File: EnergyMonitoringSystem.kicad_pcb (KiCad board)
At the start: 6 copper layers, 170 x 117 mm, 202 parts, among them J201 USB_C_Receptacle_USB2.0_16P, J202 Screw_Terminal_01x02, J401 Conn_02x05_Counter_Clockwise, J402 Conn_02x05_Counter_Clockwise, J403 Conn_02x08_Counter_Clockwise, J501 Screw_Terminal_01x02, J502 Screw_Terminal_01x02, J503 Screw_Terminal_01x02, J504 Screw_Terminal_01x02, J505 Screw_Terminal_01x02, J506 Screw_Terminal_01x02, J601 DM3AT-SF-PEJM5_40_, J602 Screw_Terminal_01x03, Q201 STL6N3LLH6, SW401 SW_Push, SW402 SW_Push, U201 USBLC6-2P6, U202 STEF05SGR, U203 TCPP01-M12, U301 LDLN025M12R, U302 ST1PS02CQTR, U303 ST1PS02CQTR, U304 LM2664M6_NOPB, U401 STM32F103RGT6, U402 BLUENRG-M2SA, U501 ADS131M08IRSNR, U502 TSV914AIDR, U503 TSV914AIDR, U504 TSV914AIDR, U601 EMIF06-MSD02N16, U602 ADM2565EBRNZ, Y401 16MHz, Y402 32.768KHz

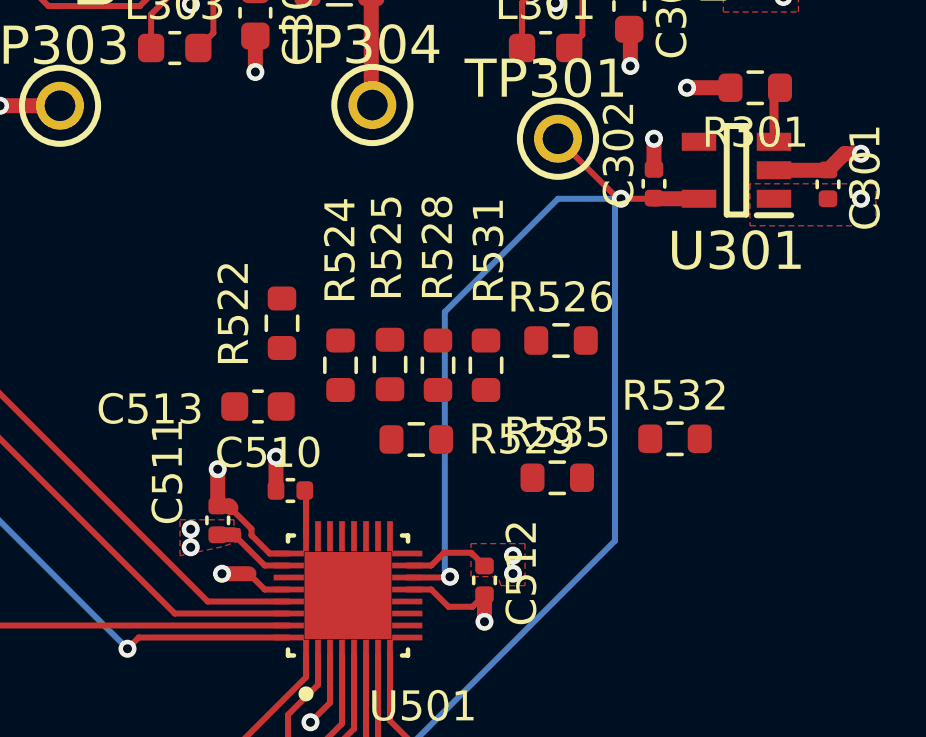
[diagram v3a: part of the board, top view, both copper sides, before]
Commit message: adc wiring complete
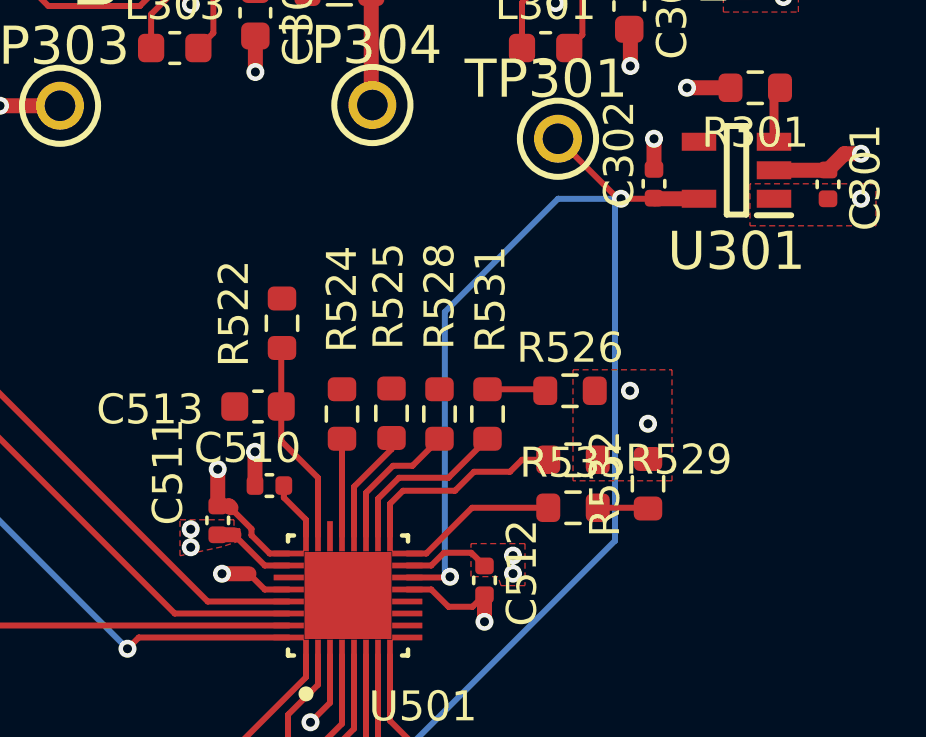
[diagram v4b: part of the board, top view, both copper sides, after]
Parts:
- moved R529 5.27 mm to (104.1, 86.7)
- moved R532 1.75 mm to (106.6, 87.5), turned to 90 degrees
- moved R526 1.70 mm to (104.0, 84.4)
- moved R524 1.63 mm to (96.4, 85.2)
- moved R528 1.63 mm to (99.7, 85.2)
- moved R525 1.63 mm to (98.0, 85.2)
- moved R531 1.63 mm to (101.2, 85.2)
- moved R535 1.13 mm to (104.1, 88.3)
- moved C510 0.72 mm to (94.0, 87.6)
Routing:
- net ADS_CS: track 0.00 -> 6.97 mm
- net /ADC/CLKIN_ADS_T: track 0.00 -> 6.79 mm
- net /ADC/DRDY_ADS_T: track 0.00 -> 5.73 mm
- net /ADC/SYNC_RESET_ADS_T: track 0.00 -> 5.33 mm
- net /ADC/SCK_ADS_T: track 0.00 -> 4.64 mm
- net /ADC/DOUT_ADS_T: track 0.00 -> 3.79 mm
- net /ADC/DIN_ADS_T: track 0.00 -> 3.25 mm
- net ADS_DRDY: track 0.00 -> 1.95 mm
- net ADS_SYNC_RESET: track 0.00 -> 1.69 mm
- net Net-(U501-CAP): track 1.54 -> 2.05 mm
- net +DCDC_1: vias 13 -> 15

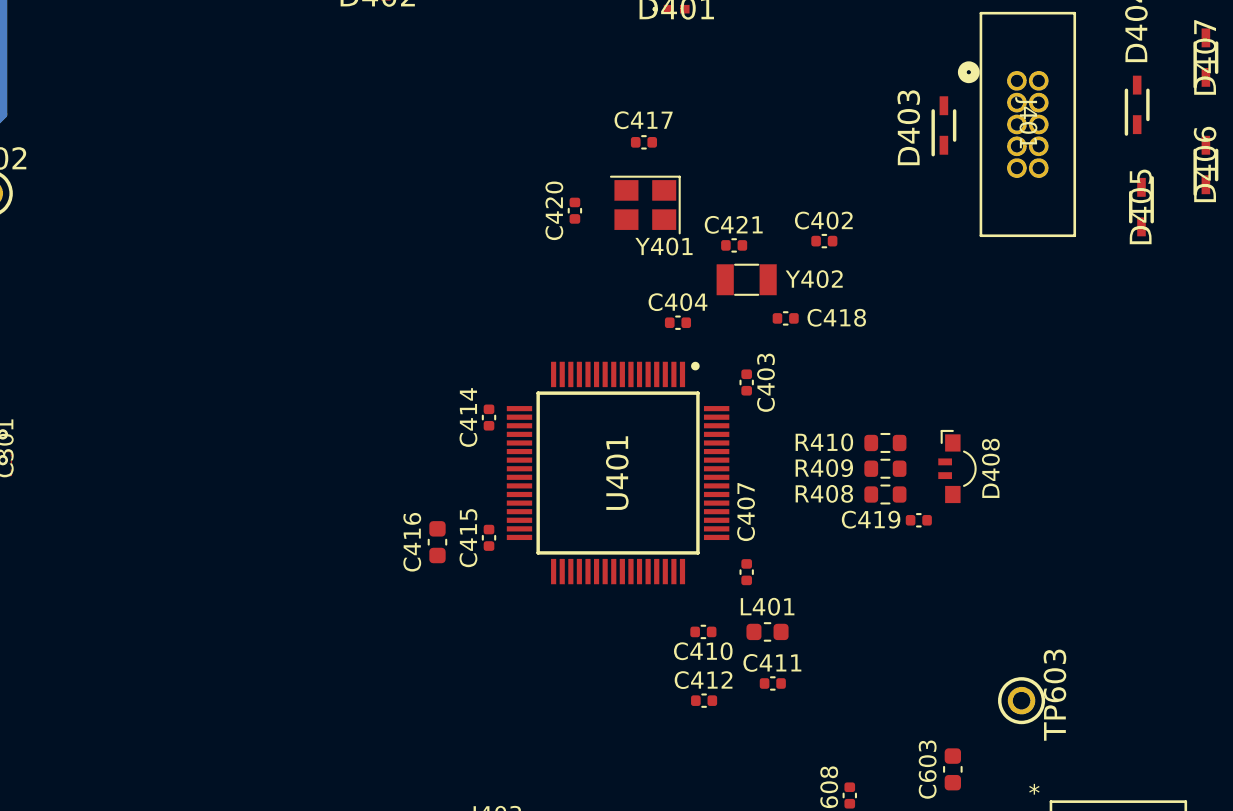
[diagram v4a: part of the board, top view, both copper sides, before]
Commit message: power supply to uC
1. Power supply complete
2. Crystal Oscillator complete
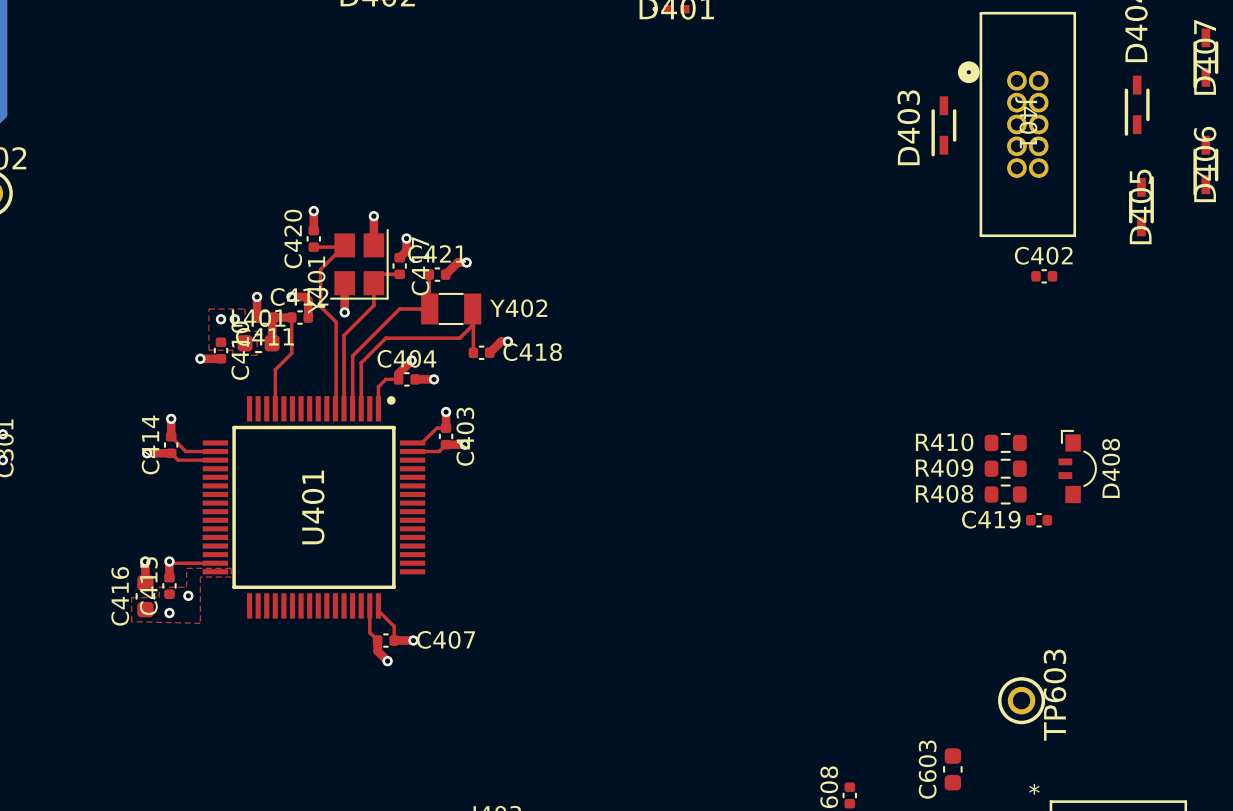
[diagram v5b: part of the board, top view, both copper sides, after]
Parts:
- moved C411 36.4 mm to (129.0, 69.7), turned to 180 degrees
- moved L401 34.1 mm to (128.6, 71.2)
- moved C410 32.5 mm to (126.4, 71.6), turned to -90 degrees
- moved C412 32.4 mm to (131.0, 69.7)
- moved C407 21.4 mm to (136.0, 88.5), turned to 180 degrees
- moved C415 18.8 mm to (123.4, 85.3)
- moved C414 18.6 mm to (123.5, 77.1)
- moved C418 17.8 mm to (141.6, 71.8)
- moved U401 17.8 mm to (131.8, 80.8)
- moved C403 17.8 mm to (139.5, 76.6)
- moved C421 17.4 mm to (139.0, 67.2)
- moved C416 17.3 mm to (122.0, 85.9)
- moved Y402 17.3 mm to (139.8, 69.2)
- moved Y401 17.0 mm to (134.4, 66.6), turned to 90 degrees
- moved C404 16.1 mm to (137.2, 73.3)
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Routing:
- net GND: track 238.3 -> 268.3 mm, vias 59 -> 74
- net +DCDC_1: track 18.3 -> 33.2 mm, vias 15 -> 23
- net /uC/OSC32_IN: track 0.00 -> 13.6 mm
- net /uC/OSC_OUT: track 0.00 -> 12.3 mm
- net /uC/OSC32_OUT: track 0.00 -> 10.7 mm
- net /uC/OSC_IN: track 0.00 -> 9.75 mm
- net VDDA: track 0.00 -> 8.30 mm

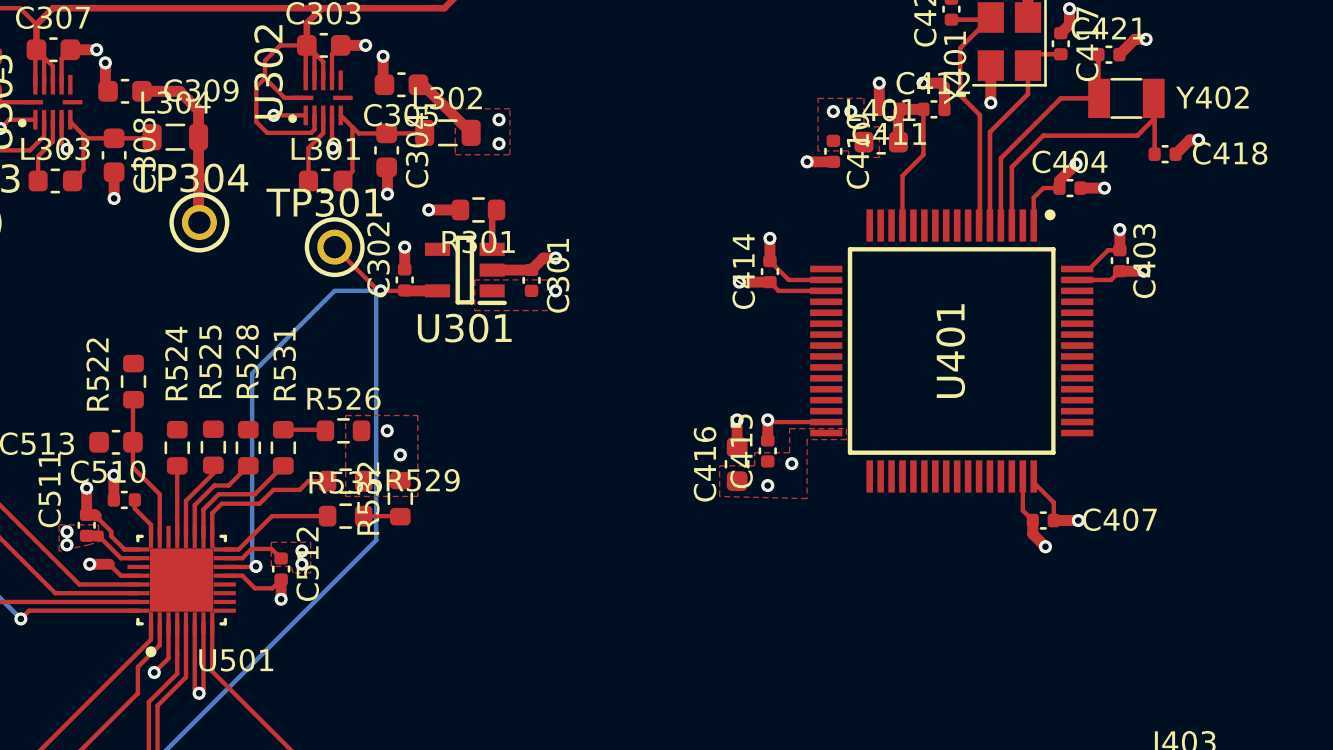
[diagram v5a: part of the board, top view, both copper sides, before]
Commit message: adc to uc complete
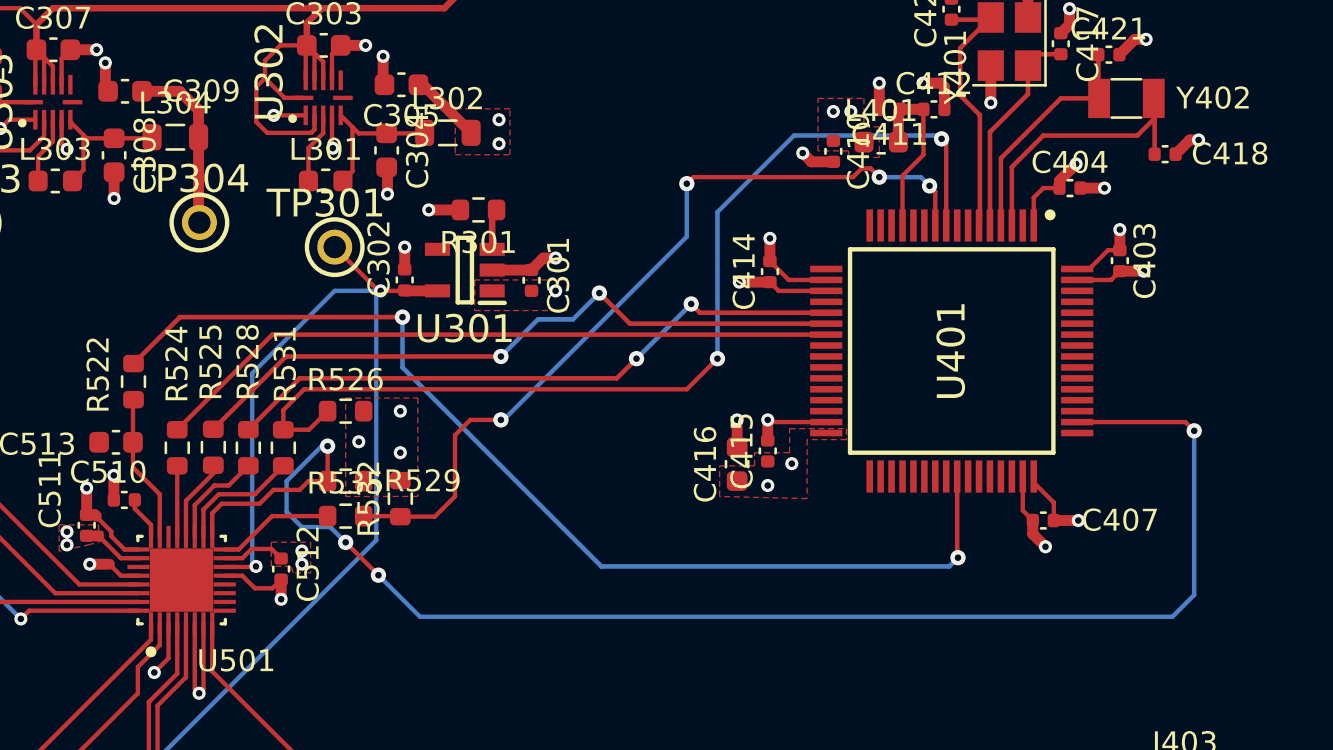
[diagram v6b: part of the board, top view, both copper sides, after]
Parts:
- moved R526 0.91 mm to (104.1, 83.5)
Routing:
- net ADS_CS: track 6.97 -> 69.4 mm, vias 0 -> 4
- net ADS_STM32_CLKOUT: track 0.00 -> 48.5 mm, vias 0 -> 2
- net ADS_DRDY: track 1.95 -> 46.6 mm, vias 0 -> 2
- net ADS_SYNC_RESET: track 1.69 -> 37.8 mm, vias 0 -> 4
- net ADS_DIN_uC_DOUT: track 0.00 -> 31.5 mm
- net ADS_DOUT_uC_DIN: track 0.00 -> 31.2 mm, vias 0 -> 2
- net ADS_SPI1_SCK: track 0.00 -> 29.0 mm, vias 0 -> 2
- net +DCDC_1: vias 23 -> 24

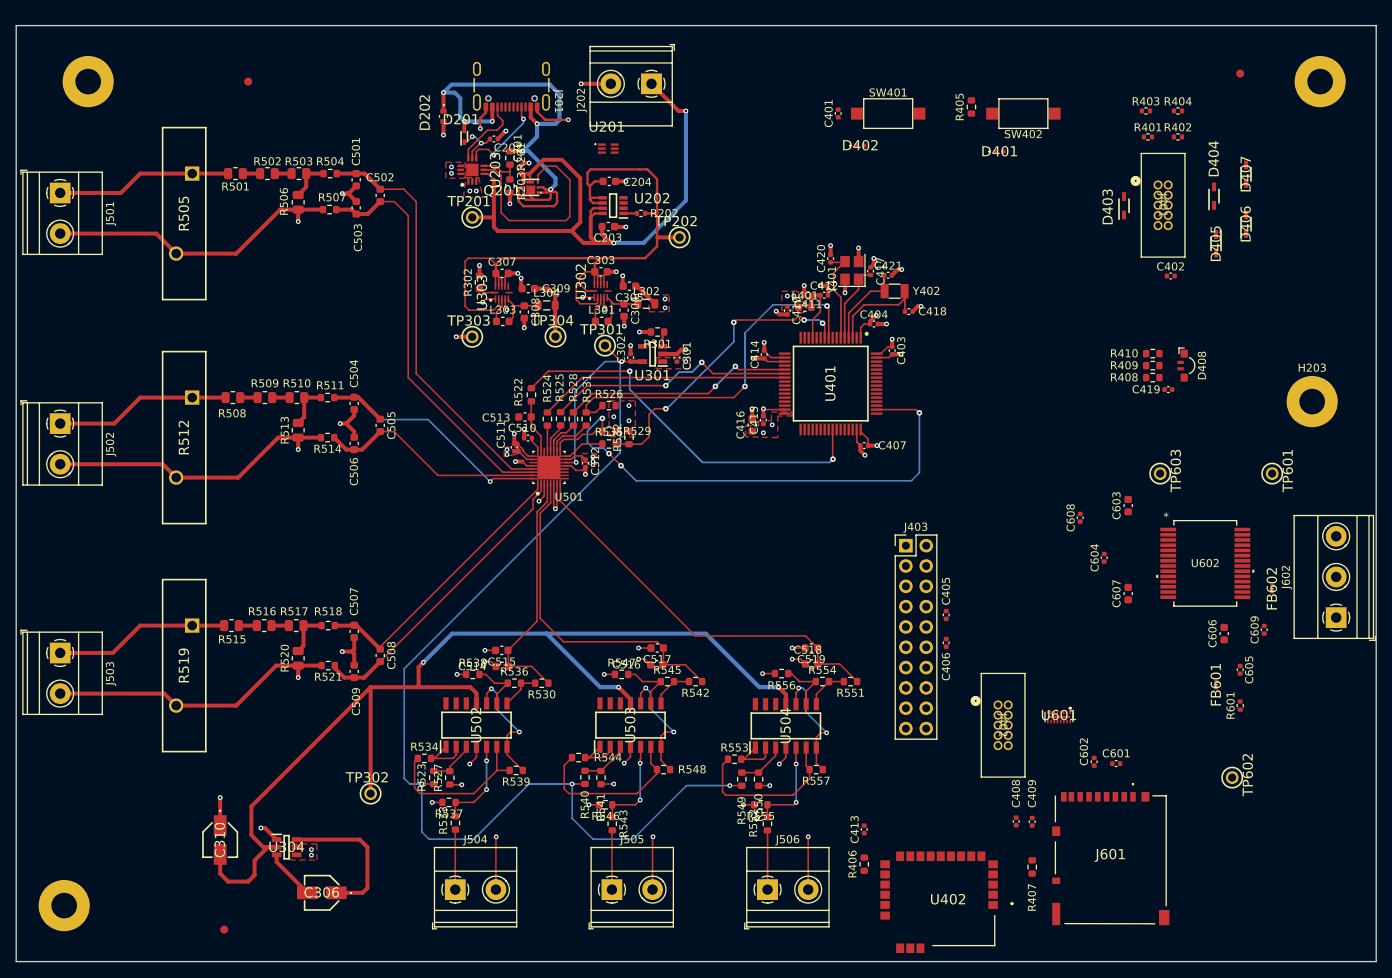
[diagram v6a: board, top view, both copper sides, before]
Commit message: routing for blueNRG complete
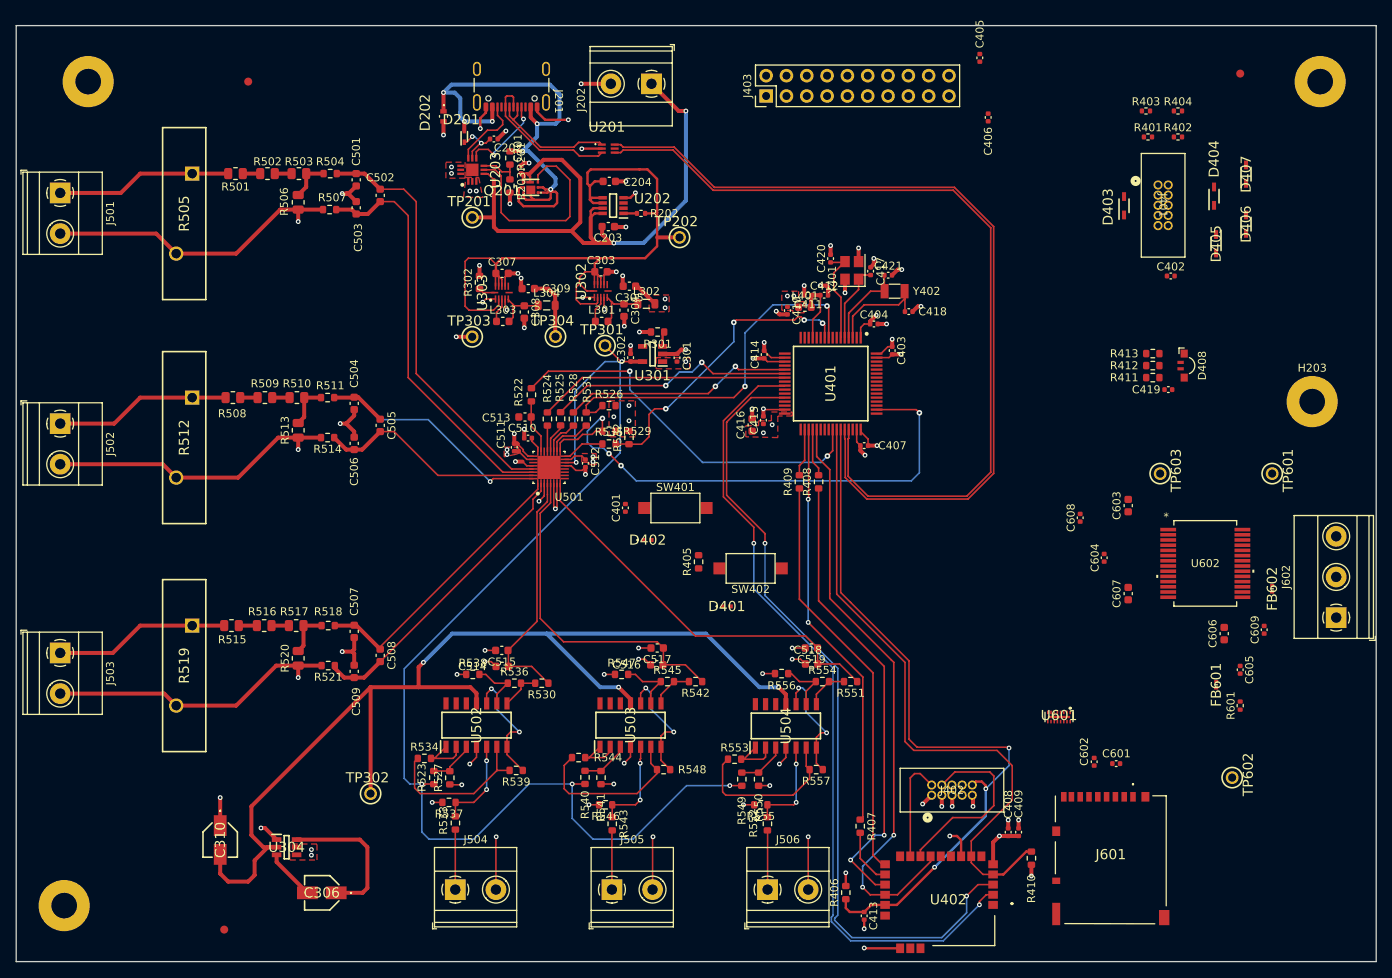
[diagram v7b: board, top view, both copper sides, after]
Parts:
- added R407: 22R, Resistor_SMD:R_0603_1608Metric, F.Cu at (135.5, 136.1)
- added R408: 22R, Resistor_SMD:R_0603_1608Metric, F.Cu at (130.3, 93.0)
- added R409: 22R, Resistor_SMD:R_0603_1608Metric, F.Cu at (127.9, 93.0)
- moved C405 69.8 mm to (150.4, 40.0)
- moved R405 66.3 mm to (115.3, 103.0)
- moved D401 66.3 mm to (118.8, 108.6)
- moved SW402 66.3 mm to (121.8, 103.8)
- moved C406 65.9 mm to (151.5, 47.5)
- moved J403 58.9 mm to (123.7, 44.8), turned to 90 degrees
- moved C401 56.0 mm to (106.2, 96.3)
- moved D402 56.0 mm to (108.9, 100.3)
- moved SW401 56.0 mm to (112.4, 96.3)
- moved J402 14.0 mm to (144.4, 132.2), turned to 0 degrees
- moved C413 10.8 mm to (136.0, 147.3), turned to -90 degrees
- moved R406 4.23 mm to (133.7, 144.4)
- moved C409 2.14 mm to (155.3, 136.8)
- moved C408 1.67 mm to (154.0, 136.8)
- moved R410 1.10 mm to (156.9, 140.1)
- renumbered R407 to R410, R408 to R411, R409 to R412, R410 to R413
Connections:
- net /USB/USB_OTG_DM renamed /USB/USB_OTG_D-
- net /USB/USB_OTG_DP renamed /USB/USB_OTG_D+
- net uC_OTG_DM renamed uC_OTG_D-
- net uC_OTG_DP renamed uC_OTG_D+
- U401 pad 34: /uC/SPI2_SCK -> /uC/SPI2_R_SCK
- U401 pad 36: /uC/SPI2_MOSI -> /uC/SPI2_R_MOSI
- U402 pad 16: /uC/SPI2_MISO -> /uC/SPI2_R_MISO
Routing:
- net uC_OTG_D-: track 0.00 -> 109.5 mm
- net uC_OTG_D+: track 0.00 -> 107.7 mm
- net /uC/BLE_TEST8: track 0.00 -> 101.7 mm, vias 0 -> 2
- net /uC/BLE_TEST9: track 0.00 -> 101.4 mm, vias 0 -> 2
- net /uC/BLE_RST: track 0.00 -> 91.2 mm, vias 0 -> 3
- net /uC/BLE_INT: track 0.00 -> 80.8 mm
- net /uC/BLE_SPI_CS: track 0.00 -> 74.1 mm, vias 0 -> 2
- net /uC/SPI2_MOSI: track 0.00 -> 57.8 mm, vias 0 -> 2
- net /uC/SPI2_MISO: track 0.00 -> 51.8 mm, vias 0 -> 2
- net /uC/SPI2_SCK: track 0.00 -> 51.6 mm
- net /uC/BLE_SWDCLK: track 0.00 -> 23.4 mm
- net GND: track 268.7 -> 290.0 mm, vias 74 -> 85
- net /USB/USB_OTG_D+: track 0.00 -> 19.0 mm
- net /USB/USB_OTG_D-: track 0.00 -> 16.5 mm
- net /uC/BLE_SWDIO: track 0.00 -> 13.3 mm
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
